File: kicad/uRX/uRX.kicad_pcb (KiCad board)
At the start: 2 copper layers, 181 parts, among them J1 RF_AM_GND, J10 GPIO_A, J11 Bat1, J12 TPH, J2 C165948, J3 Loudspeaker, J4 Display, J5 e-ink, J6 U.FL, J7 GPS, J8 Bat0, J9 RF_AM__In, Q1 BC847, Q2 BC847, Q3 BC847, SW1 RotaryEncoder_Switch, SW2 SW_DPDT_x2, SW3 Reset, SW4 Boot, U1 CBT3253, U10 IP2326, U11 LP2985-5.0, U12 OPA2211, U13 HT733333, U2 LM4562, U3 PAM8406D, U4 Si5351A-B-GT, U5 ESP32-S3-WROOM-2, U6 Si4732-A10, U7 PCM1808PWR, U8 LM4040-2.5, U9 PCM1808PWR, X1 X322525MOB4SI, Y2 32768kHz

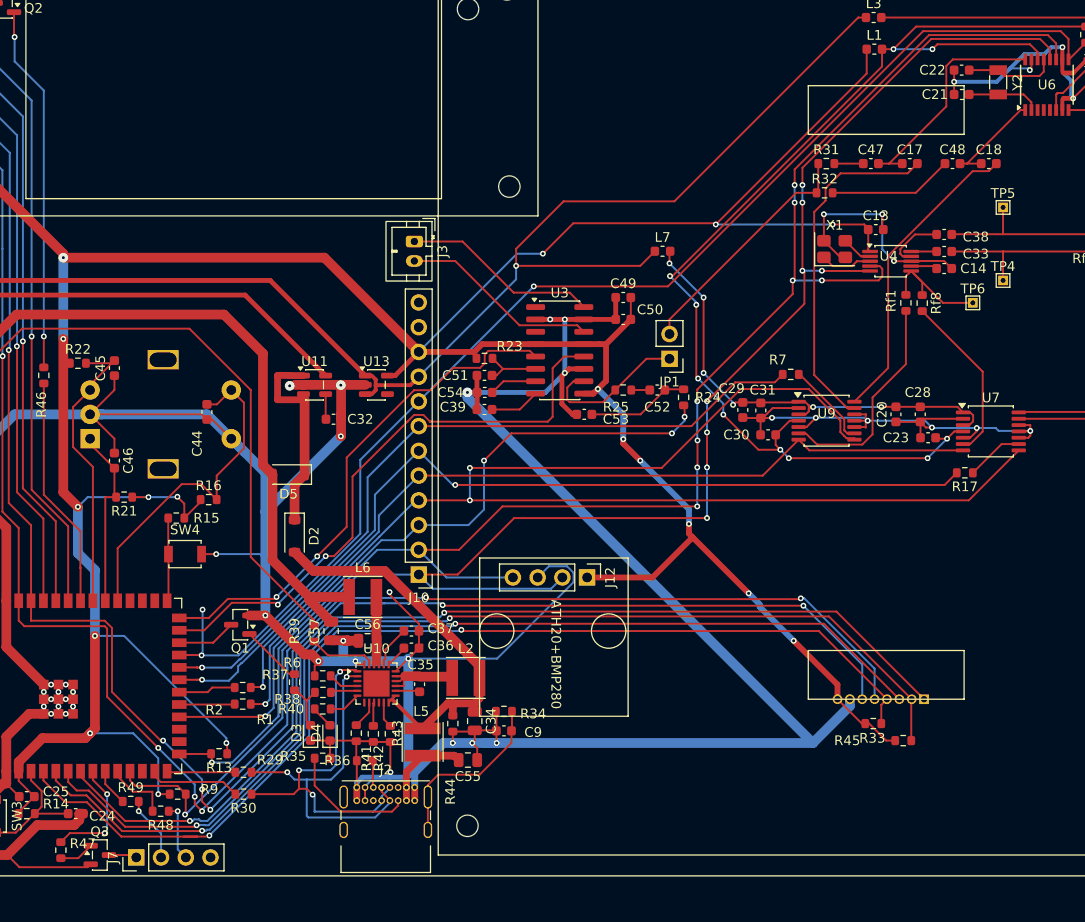
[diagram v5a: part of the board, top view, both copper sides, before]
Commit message: add dac
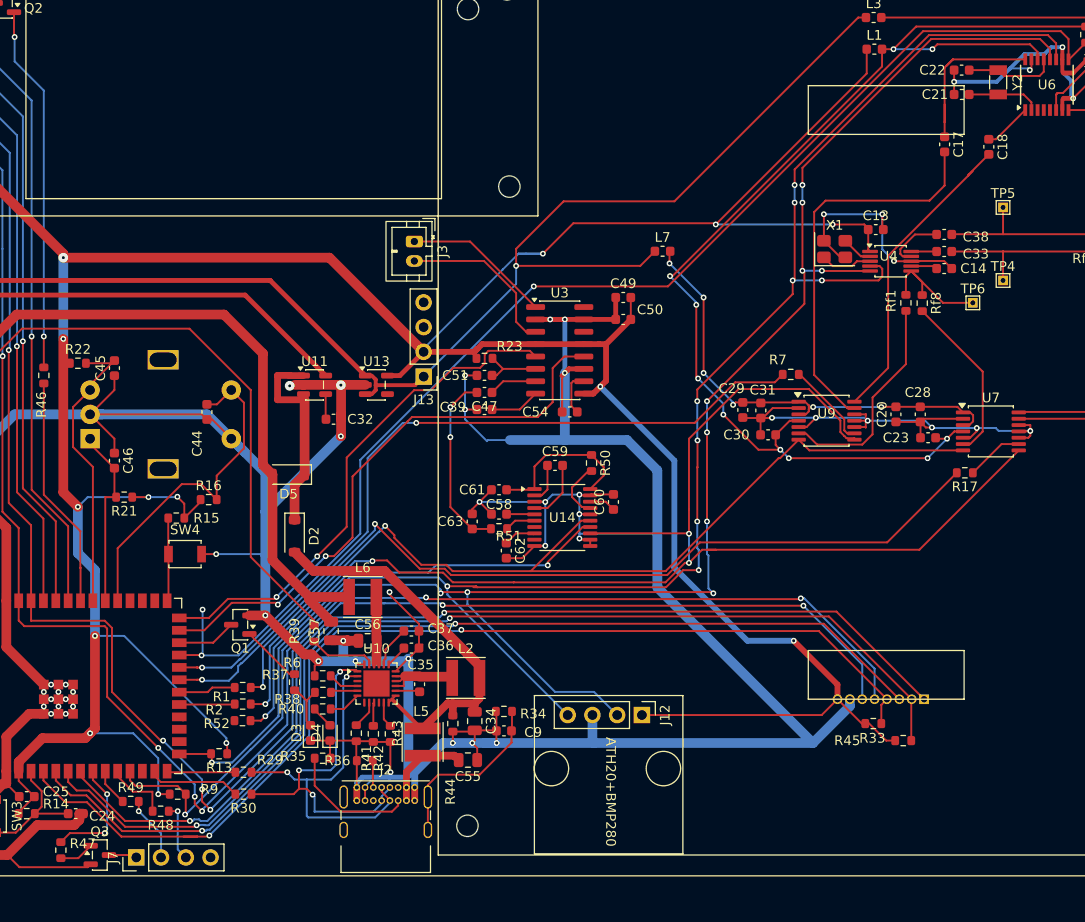
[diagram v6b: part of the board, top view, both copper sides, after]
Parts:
- removed C48, C52: 1u, Capacitor_SMD:C_0603_1608Metric
- removed C53: 10n, Capacitor_SMD:C_0603_1608Metric
- removed J10: GPIO_A, Connector_PinHeader_2.54mm:PinHeader_1x12_P2.54mm_Vertical
- removed JP1: AudioMix, Connector_PinHeader_2.54mm:PinHeader_1x02_P2.54mm_Vertical
- removed R24, R25, R31, R32: 1k, Resistor_SMD:R_0603_1608Metric
- added C58: 2.2u, Capacitor_SMD:C_0603_1608Metric, F.Cu at (138.2, 102.0)
- added C59: 2.2u, Capacitor_SMD:C_0603_1608Metric, F.Cu at (144.0, 97.0)
- added C60: 2.2u, Capacitor_SMD:C_0603_1608Metric, F.Cu at (150.0, 100.7)
- added C61: 100n, Capacitor_SMD:C_0603_1608Metric, F.Cu at (138.2, 99.5)
- added C62: 10u, Capacitor_SMD:C_0603_1608Metric, F.Cu at (139.0, 105.7)
- added C63: 2.2n, Capacitor_SMD:C_0603_1608Metric, F.Cu at (135.5, 102.7)
- added J13: Power, Connector_PinHeader_2.54mm:PinHeader_1x04_P2.54mm_Vertical, F.Cu at (130.5, 87.9)
- added R50: 10k, Resistor_SMD:R_0603_1608Metric, F.Cu at (147.7, 96.7)
- added R51: 470, Resistor_SMD:R_0603_1608Metric, F.Cu at (138.2, 103.5)
- added R52: 22, Resistor_SMD:R_0603_1608Metric, F.Cu at (111.9, 123.2)
- added U14: PCM5102A, Package_SO:TSSOP-20_4.4x6.5mm_P0.65mm, F.Cu at (144.7, 102.3)
- C47: value 1u -> 4.7u
- moved C47 46.1 mm to (136.8, 89.5), turned to 180 degrees
- moved J12 15.2 mm to (152.9, 122.6)
- moved C54 8.95 mm to (145.5, 91.5)
- moved C17 4.08 mm to (184.0, 64.0), turned to -90 degrees
- moved C18 1.72 mm to (188.5, 64.3), turned to -90 degrees
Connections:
- net /I2S0_DOUT renamed /I2S_DIN0
- net /I2S1_DOUT renamed /I2S_DIN1
- C47 pad 1: Net-(C47-Pad1) -> Net-(U3-INL)
- C47 pad 2: Net-(U6-ROut) -> /AUDIO_MONO_DAC
- C54 pad 2: Net-(U3-INL) -> Net-(U3-INR)
- J3 pad 2: Net-(J3-Pin_2) -> unconnected-(J3-Pin_2-Pad2)
- U3 pad 1: unconnected-(U3-+OUT_L-Pad1) -> Net-(J3-Pin_1)
- U3 pad 10: Net-(JP1-A) -> Net-(U3-INR)
- U3 pad 14: Net-(J3-Pin_2) -> unconnected-(U3--OUT_R-Pad14)
- U3 pad 16: Net-(J3-Pin_1) -> unconnected-(U3-+OUT_R-Pad16)
- U5 pad 18: /AUDIO_MONO_ESP -> Net-(U5-GPIO10/TOUCH10/ADC1_CH9/FSPICS0/FSPIIO4/SUBSPICS0)
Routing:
- net /AUDIO_MONO_ESP: track 72.5 -> 0.00 mm, vias 4 -> 0
- net /I2S_DOUT: track 0.00 -> 46.9 mm, vias 0 -> 2
- net +3.3V: track 350.9 -> 385.5 mm, vias 18 -> 14
- net GND: track 745.5 -> 771.3 mm, vias 53 -> 60
- net /AUDIO_MONO_4732: track 24.8 -> 0.00 mm
- net Net-(J3-Pin_2): track 20.4 -> 0.00 mm
- net /AUDIO_MONO_DAC: track 0.00 -> 18.7 mm, vias 0 -> 2
- net (no net): track 0.00 -> 17.2 mm
- net Net-(JP1-A): track 15.7 -> 0.00 mm
- net Net-(C48-Pad1): track 12.8 -> 0.00 mm
- net /SCL: track 164.7 -> 177.5 mm, vias 9 -> 10
- net /SDA: track 175.0 -> 187.0 mm, vias 9 -> 11
- net /I2S_LRCK: track 87.4 -> 98.9 mm, vias 1 -> 2
- net Net-(C52-Pad1): track 10.4 -> 0.00 mm
- net Net-(U14-CAPM): track 0.00 -> 6.35 mm
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
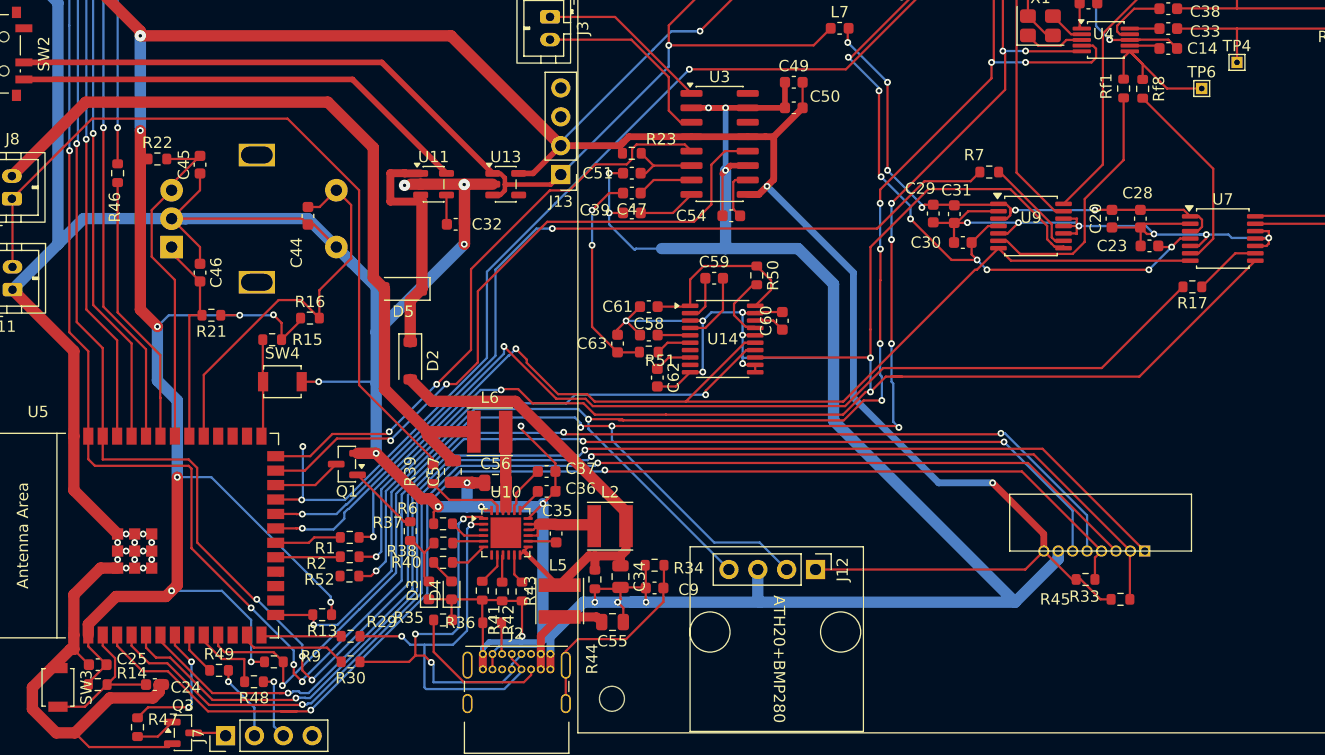
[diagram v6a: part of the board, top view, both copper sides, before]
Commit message: esp verify code compiled
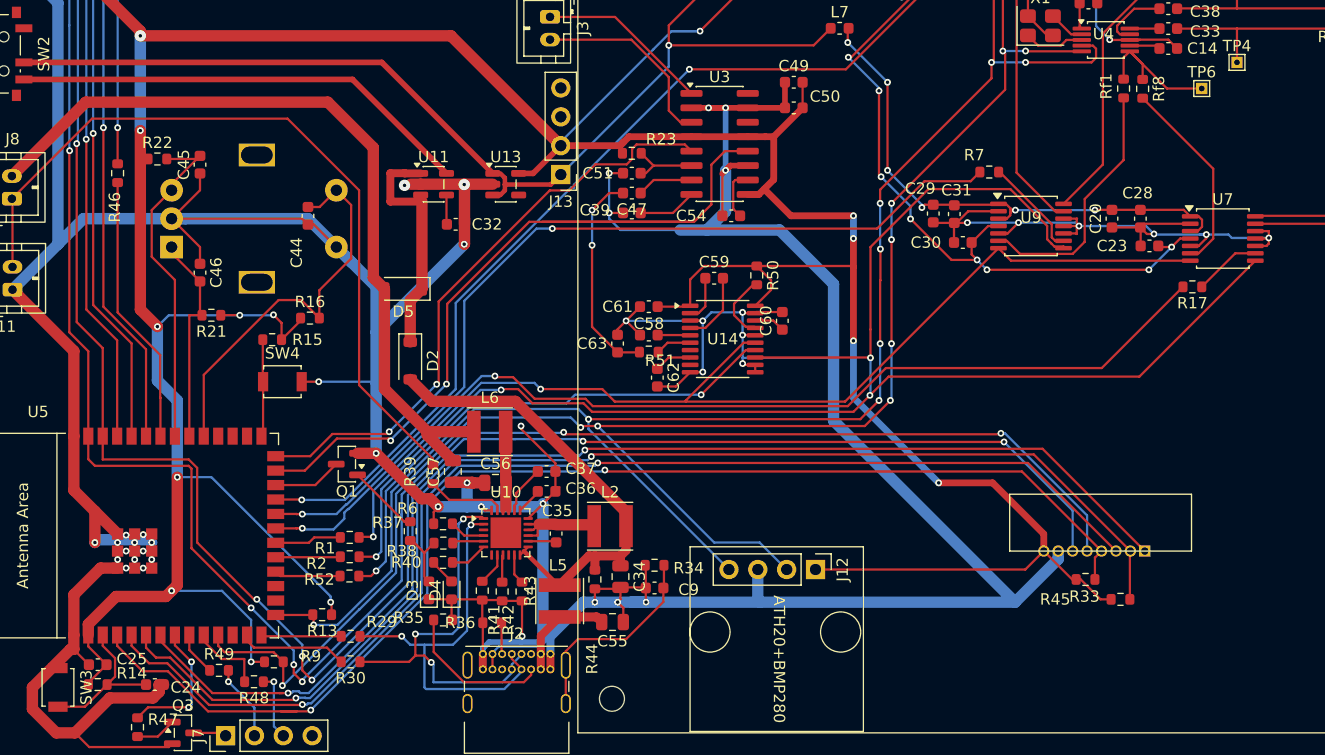
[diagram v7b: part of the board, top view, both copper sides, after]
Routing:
- net /AUDIO_SHND: track 59.1 -> 73.3 mm
- net +3.3V: track 385.5 -> 397.1 mm, vias 14 -> 16
- net GND: track 771.3 -> 777.9 mm, vias 60 -> 73
- net Net-(U5-GPIO10/TOUCH10/ADC1_CH9/FSPICS0/FSPIIO4/SUBSPICS0): track 0.54 -> 5.82 mm
- net RST_4732: track 131.9 -> 127.5 mm, vias 3 -> 2
- net /I2S_LRCK: track 98.9 -> 96.3 mm
- net /I2S_DIN0: track 93.8 -> 91.2 mm
- net /SDA: track 187.0 -> 184.9 mm
- net /I2S_BCK: track 140.6 -> 139.8 mm
- net /SCL: track 177.5 -> 176.8 mm
- net +5VfilteredM: vias 18 -> 6
